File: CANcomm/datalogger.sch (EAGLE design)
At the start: 44 parts, among them J1 MICRO-SD_CARD_SOCKET, Y1 16MHz, Y2 32.768kHz

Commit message: Make board
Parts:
- PROGUSB: value (none) -> USB_MINI-B_SMT; device SparkFun-Connectors:USB_MICRO-B_FEMALE-SMT -> SparkFun-Connectors:USB_MINI-B_SMT
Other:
- moved on the sheet: PROGUSB
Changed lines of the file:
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@@
 <class number="0" name="default" width="0" drill="0">
+</class>
+<class number="1" name="THICC" width="0.4064" drill="0">
 </class>
 </classes>
@@
 <part name="C8" library="SparkFun-Capacitors" library_urn="urn:adsk.eagle:library:510" deviceset="0.1UF" device="-0603-25V-(+80/-20%)" package3d_urn="urn:adsk.eagle:package:37414/1" value="0.1uF"/>
 <part name="C9" library="SparkFun-Capacitors" library_urn="urn:adsk.eagle:library:510" deviceset="0.1UF" device="-0603-25V-(+80/-20%)" package3d_urn="urn:adsk.eagle:package:37414/1" value="0.1uF"/>
-<part name="PROGUSB" library="SparkFun-Connectors" library_urn="urn:adsk.eagle:library:513" deviceset="USB_MICRO-B" device="_FEMALE-SMT" package3d_urn="urn:adsk.eagle:package:38238/1"/>
+<part name="PROGUSB" library="SparkFun-Connectors" library_urn="urn:adsk.eagle:library:513" deviceset="USB_MINI-B" device="_SMT" package3d_urn="urn:adsk.eagle:package:38244/1"/>
 <part name="SUPPLY3" library="SparkFun-PowerSymbols" library_urn="urn:adsk.eagle:library:530" deviceset="VCC" device=""/>
 <part name="GND4" library="SparkFun-PowerSymbols" library_urn="urn:adsk.eagle:library:530" deviceset="GND" device=""/>

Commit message: More work
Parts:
- PROGUSB: value USB_MINI-B_SMT -> (none); device SparkFun-Connectors:USB_MINI-B_SMT -> SparkFun-Connectors:USB_MICRO-B_FEMALE-SMT
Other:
- moved on the sheet: PROGUSB
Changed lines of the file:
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@@
 <part name="C8" library="SparkFun-Capacitors" library_urn="urn:adsk.eagle:library:510" deviceset="0.1UF" device="-0603-25V-(+80/-20%)" package3d_urn="urn:adsk.eagle:package:37414/1" value="0.1uF"/>
 <part name="C9" library="SparkFun-Capacitors" library_urn="urn:adsk.eagle:library:510" deviceset="0.1UF" device="-0603-25V-(+80/-20%)" package3d_urn="urn:adsk.eagle:package:37414/1" value="0.1uF"/>
-<part name="PROGUSB" library="SparkFun-Connectors" library_urn="urn:adsk.eagle:library:513" deviceset="USB_MINI-B" device="_SMT" package3d_urn="urn:adsk.eagle:package:38244/1"/>
+<part name="PROGUSB" library="SparkFun-Connectors" library_urn="urn:adsk.eagle:library:513" deviceset="USB_MICRO-B" device="_FEMALE-SMT" package3d_urn="urn:adsk.eagle:package:38238/1"/>
 <part name="SUPPLY3" library="SparkFun-PowerSymbols" library_urn="urn:adsk.eagle:library:530" deviceset="VCC" device=""/>
 <part name="GND4" library="SparkFun-PowerSymbols" library_urn="urn:adsk.eagle:library:530" deviceset="GND" device=""/>

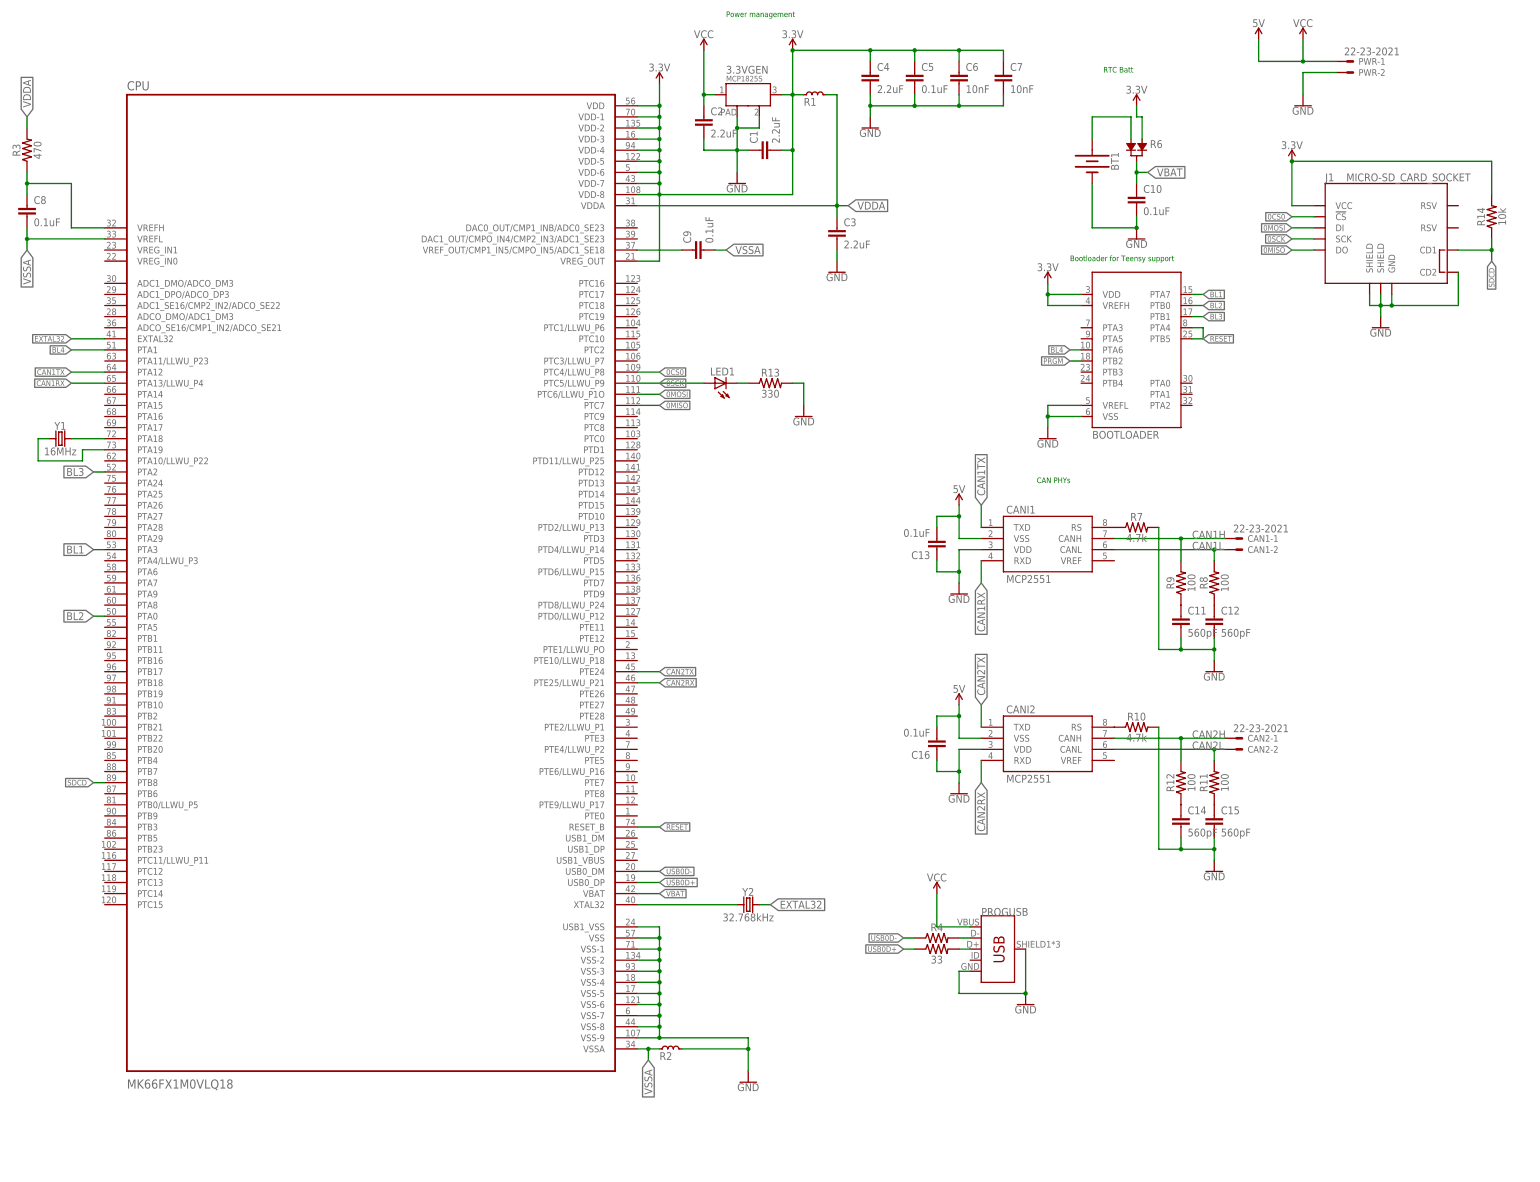
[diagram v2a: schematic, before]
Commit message: Add USB-C and PRGM button
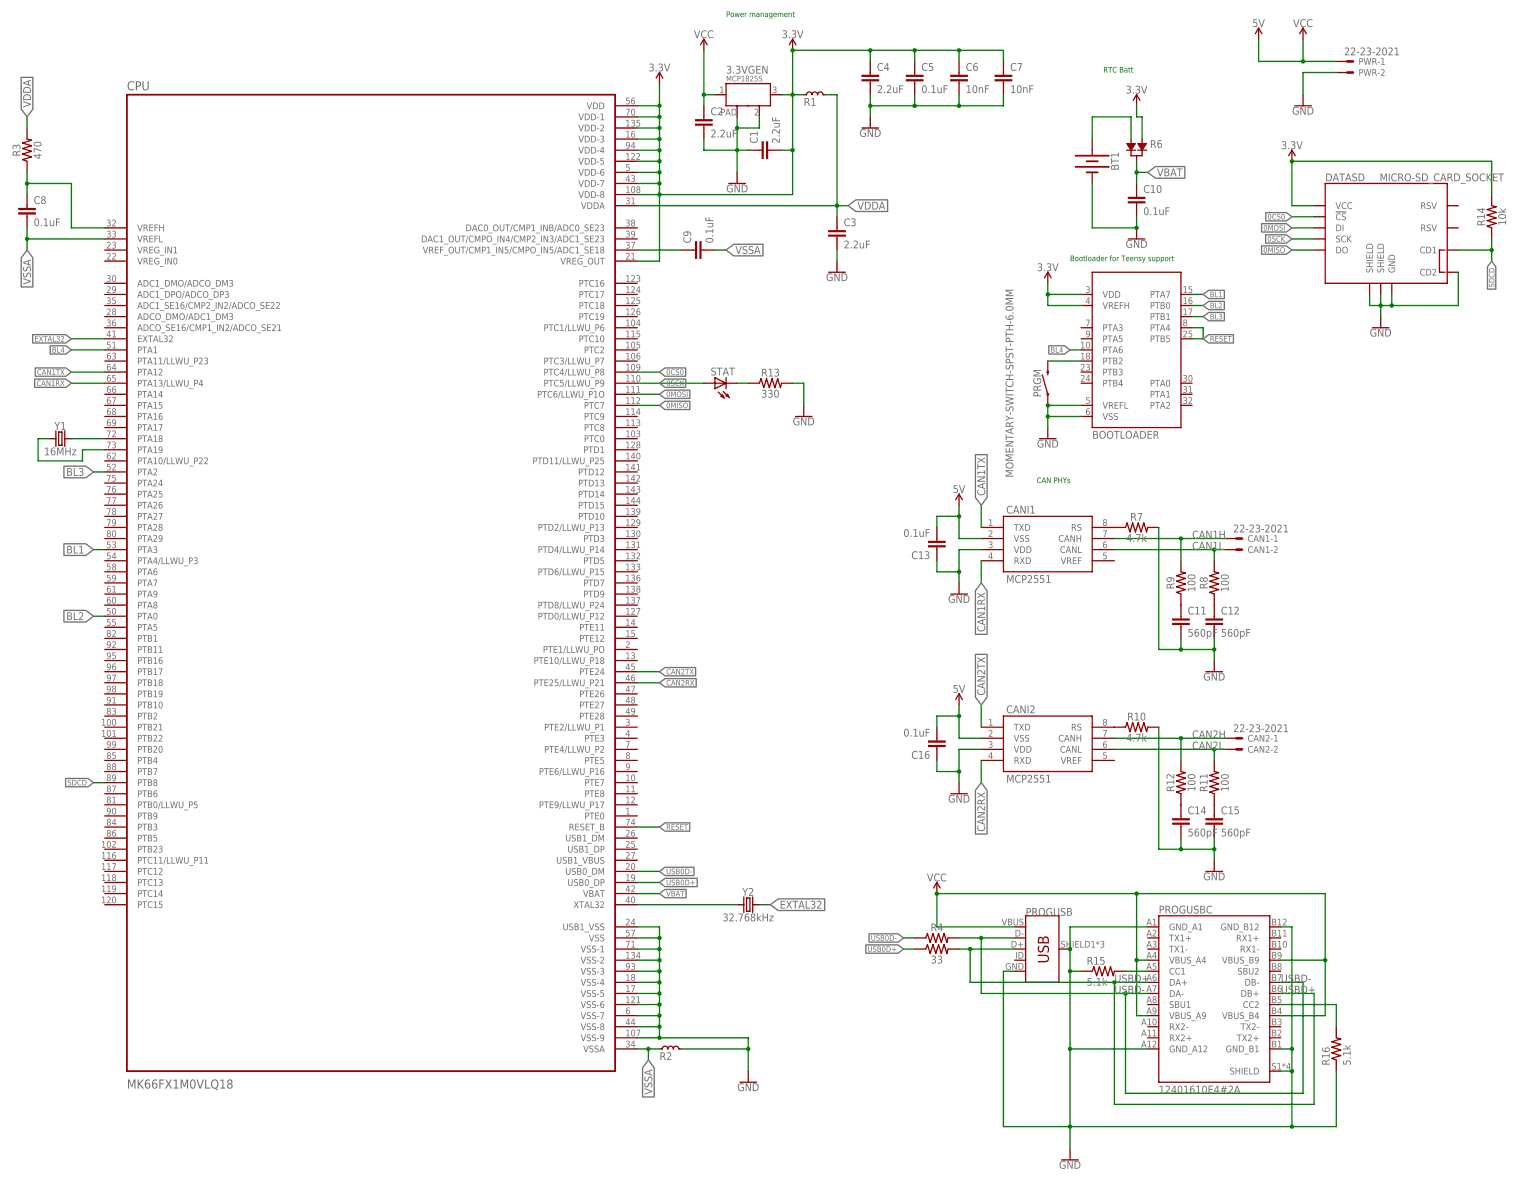
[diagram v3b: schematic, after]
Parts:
- added PRGM: MOMENTARY-SWITCH-SPST-PTH-6.0MM, SparkFun-Switches:MOMENTARY-SWITCH-SPST-PTH-6.0MM
- added PROGUSBC: 12401610E4#2A, 12401610E4_2A:12401610E4#2A
- added R15, R16: 5.1k, rcl:R-US_R0603
- renumbered J1 to DATASD, LED1 to STAT
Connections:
- removed net N$6: PROGUSB.D-, R4.2
- removed net N$7: PROGUSB.D+, R5.2
- new net N$11: PROGUSBC.CC2, R16.2
- new net N$9: PROGUSBC.CC1, R15.2
- new net USBD+: PROGUSB.D+, PROGUSBC.DA+, PROGUSBC.DB+, R5.2
- new net USBD-: PROGUSB.D-, PROGUSBC.DA-, PROGUSBC.DB-, R4.2
- net GND: now also PRGM.1, PROGUSBC.GND_A1, PROGUSBC.GND_A12, PROGUSBC.GND_B1, PROGUSBC.GND_B12, PROGUSBC.SHIELD, R15.1, R16.1
- net PRGM: now also PRGM.2
- net VCC: now also PROGUSBC.VBUS_A4, PROGUSBC.VBUS_A9, PROGUSBC.VBUS_B4, PROGUSBC.VBUS_B9
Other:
- moved on the sheet: PROGUSB
